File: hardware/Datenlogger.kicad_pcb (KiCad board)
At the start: 2 copper layers, 70 x 50 mm, 58 parts, among them J1 AVR-ISP-6, J10 I2C0, J11 I2C1, J12 I2C2, J2 PWR, J3 Measure0, J4 Measure1, J5 serial, J6 SPI0, J7 SPI1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

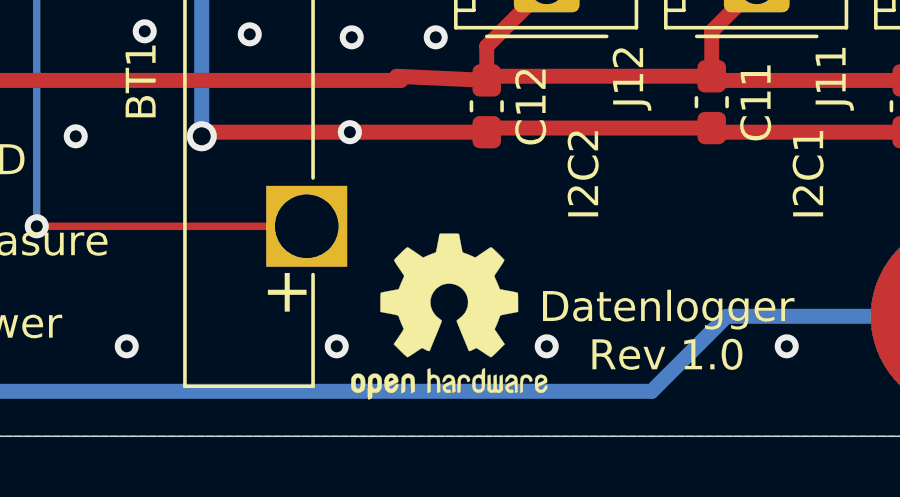
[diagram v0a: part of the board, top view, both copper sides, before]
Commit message: Updated oscilator to be suited for standard UART baudrates.
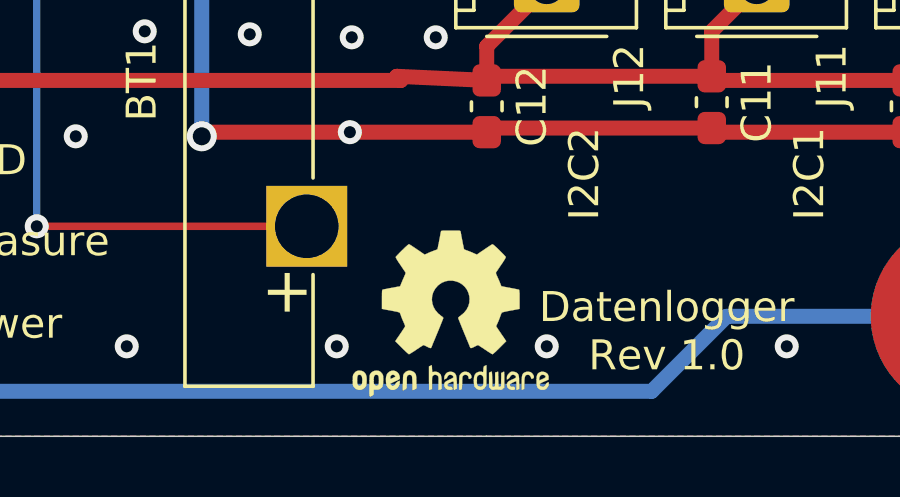
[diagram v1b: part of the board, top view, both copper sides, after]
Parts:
- Y1: value 8.192MHz -> 11.0592MHz
- moved REF** 0.11 mm to (208.8, 105.9)

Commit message: fix: Minor fixes to the hardware
Corrected text on allowed voltages to 2.6V-3.6V caused by the limits of the flash device.
Modified value of R1 to 56Ohm as the original was clearly way too high.

fixes #1
fixes #2
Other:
- board text added: "2,5-3.6V"
- board text removed: "2,5-5V"

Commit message: Fundamental HW Fix, added testsuite
* fix #3  missing I2C connections
* fix #4  different components for R1/C1 to ensure switch-over to battery
* add extensive testsuite hwtest used to verify the HW.
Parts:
- C1: value 100nF -> 2.2uF
- R1: value 1k -> 22
- moved REF** 0.10 mm to (208.8, 105.8)
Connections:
- R3 pad 2: /SCL -> /I2C_SCL
- R4 pad 2: /SDA -> /I2C_SDA
- U2 pad 27: /SDA -> /I2C_SDA
- U2 pad 28: /SCL -> /I2C_SCL
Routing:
- net /I2C_SDA: track 31.5 -> 53.5 mm, vias 0 -> 2
- net /I2C_SCL: track 32.7 -> 51.2 mm, vias 0 -> 2
- net /SDA: track 6.86 -> 0.00 mm
- net /SCL: track 5.28 -> 0.00 mm
- net /nReset: track 41.1 -> 41.9 mm
- net /AD1_MEASURE: track 18.6 -> 19.2 mm
- net GND: track 403.4 -> 402.9 mm, vias 106 -> 105
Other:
- board text added: "Datenlogger Rev 1.1"
- board text added: "Datenlogger Rev 1.1 M.Staudenmaier"
- board text removed: "Datenlogger Rev 1.0"
- board text removed: "Datenlogger Rev 1.0 M.Staudenmaier"
